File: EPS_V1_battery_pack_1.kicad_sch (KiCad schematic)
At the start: 16 parts, among them U1 MP2672AGD-0000-Z

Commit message: Minor fixes
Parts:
- R_MID: value 10k -> 0
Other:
- note added: "can't find value of R_MID on datasheet anywhere so I put 0 for now"
- note removed: "can't find value of R_MID on datasheet anywhere so I guessed 10k?"
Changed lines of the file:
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@@
 		)
 	)
-	(text "can't find value of R_MID on datasheet anywhere so I guessed 10k?"
+	(text "can't find value of R_MID on datasheet anywhere so I put 0 for now"
 		(exclude_from_sim no)
 		(at 156.21 134.366 0)
@@
 			)
 		)
-		(property "Value" "10k"
+		(property "Value" "0"
 			(at 122.682 86.36 0)
 			(effects

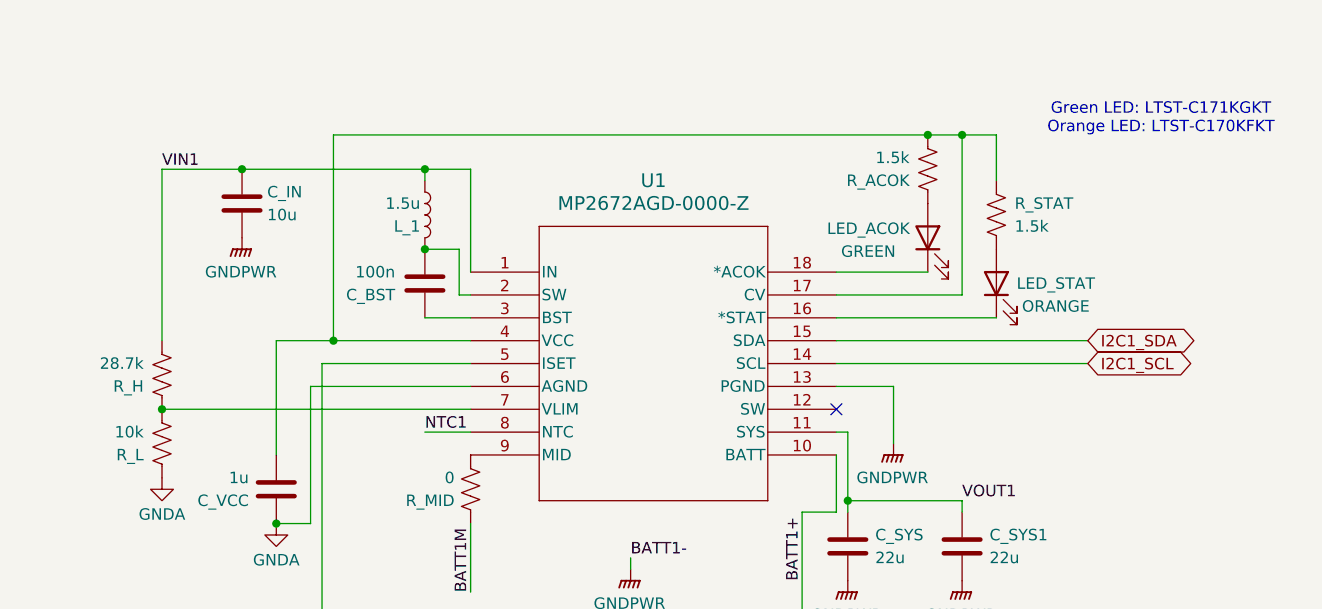
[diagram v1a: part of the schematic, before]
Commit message: Add solar to charger buck-boost converter, make charger standalone instead of host control
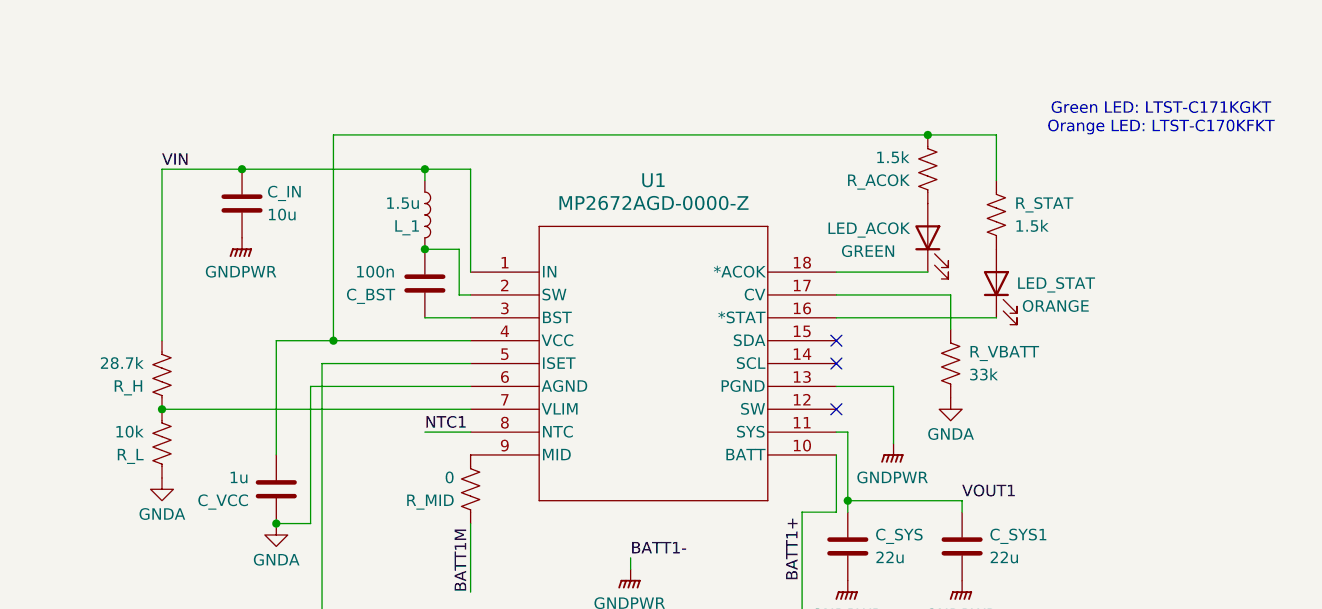
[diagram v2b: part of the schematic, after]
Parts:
- added R_VBATT: 33k, symbol Device:R_US
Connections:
- net GNDA: now also R_VBATT.2
- net at C_VCC.2, R_ACOK.2, R_STAT.1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: no longer U1.17 (CV)
- net I2C1_SCL: no longer names the net of U1.14 (SCL)
- net I2C1_SDA: no longer names the net of U1.15 (SDA)
- net VIN1 renamed VIN
- new net: R_VBATT.1, U1.17 (CV)
- no-connect marks 1 -> 3
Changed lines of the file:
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@@
-	)
-	(junction
-		(at 179.07 48.26)
-		(diameter 0)
-		(color 0 0 0 0)
 	)
 	(junction
@@
 		(at 165.1 78.74)
 	)
+	(no_connect
+		(at 165.1 73.66)
+	)
+	(no_connect
+		(at 165.1 71.12)
+	)
 	(wire
 		(pts
@@
 	(wire
 		(pts
-			(xy 182.88 48.26) (xy 179.07 48.26)
+			(xy 175.26 48.26) (xy 182.88 48.26)
 		)
 		(stroke
@@
 	(wire
 		(pts
+			(xy 177.8 66.04) (xy 177.8 69.85)
+		)
+		(stroke
+			(width 0)
+			(type default)
+		)
+	)
+	(wire
+		(pts
 			(xy 166.37 88.9) (xy 166.37 90.17)
 		)
@@
 	(wire
 		(pts
-			(xy 165.1 73.66) (xy 193.04 73.66)
-		)
-		(stroke
-			(width 0)
-			(type default)
-		)
-	)
-	(wire
-		(pts
 			(xy 109.22 71.12) (xy 124.46 71.12)
 		)
@@
 	(wire
 		(pts
-			(xy 179.07 48.26) (xy 175.26 48.26)
-		)
-		(stroke
-			(width 0)
-			(type default)
-		)
-	)
-	(wire
-		(pts
-			(xy 165.1 66.04) (xy 179.07 66.04)
-		)
-		(stroke
-			(width 0)
-			(type default)
-		)
-	)
-	(wire
-		(pts
 			(xy 165.1 68.58) (xy 182.88 68.58)
 		)
@@
 	(wire
 		(pts
-			(xy 179.07 66.04) (xy 179.07 48.26)
-		)
-		(stroke
-			(width 0)
-			(type default)
-		)
-	)
-	(wire
-		(pts
 			(xy 90.17 78.74) (xy 124.46 78.74)
 		)
@@
 	(wire
 		(pts
-			(xy 165.1 71.12) (xy 193.04 71.12)
-		)
-		(stroke
-			(width 0)
-			(type default)
-		)
-	)
-	(wire
-		(pts
 			(xy 166.37 81.28) (xy 166.37 88.9)
 		)
@@
 	(wire
 		(pts
+			(xy 165.1 66.04) (xy 177.8 66.04)
+		)
+		(stroke
+			(width 0)
+			(type default)
+		)
+	)
+	(wire
+		(pts
 			(xy 90.17 52.07) (xy 99.06 52.07)
 		)
@@
 		)
 	)
-	(label "VIN1"
+	(label "VIN"
 		(at 90.17 52.07 0)
 		(effects
@@
 			)
 			(justify left bottom)
-		)
-	)
-	(global_label "I2C1_SCL"
-		(shape bidirectional)
-		(at 193.04 73.66 0)
-		(fields_autoplaced yes)
-		(effects
-			(font
-				(size 1.27 1.27)
-			)
-			(justify left)
-		)
-		(property "Intersheetrefs" "${INTERSHEET_REFS}"
-			(at 205.9055 73.66 0)
-			(effects
-				(font
-					(size 1.27 1.27)
-				)
-				(justify left)
-				(hide yes)
-			)
-		)
-	)
-	(global_label "I2C1_SDA"
-		(shape bidirectional)
-		(at 193.04 71.12 0)
-		(fields_autoplaced yes)
-		(effects
-			(font
-				(size 1.27 1.27)
-			)
-			(justify left)
-		)
-		(property "Intersheetrefs" "${INTERSHEET_REFS}"
-			(at 205.966 71.12 0)
-			(effects
-				(font
-					(size 1.27 1.27)
-				)
-				(justify left)
-				(hide yes)
-			)
 		)
 	)
@@
 				(path "/85157432-5d03-48fa-ab40-27ed3d133f47/d6a7ca1d-fe68-467f-8233-74a5cf811189"
 					(reference "L_1")
+					(unit 1)
+				)
+			)
+		)
+	)
+	(symbol
+		(lib_id "Device:R_US")
+		(at 177.8 73.66 0)
+		(unit 1)
+		(exclude_from_sim no)
+		(in_bom yes)
+		(on_board yes)
+		(dnp no)
+		(property "Reference" "R_VBATT"
+			(at 179.832 72.39 0)
+			(effects
+				(font
+					(size 1.27 1.27)
+				)
+				(justify left)
+			)
+		)
+		(property "Value" "33k"
+			(at 179.832 74.93 0)
+			(effects
+				(font
+					(size 1.27 1.27)
+				)
+				(justify left)
+			)
+		)
+		(property "Footprint" ""
+			(at 178.816 73.914 90)
+			(effects
+				(font
+					(size 1.27 1.27)
+				)
+				(hide yes)
+			)
+		)
+		(property "Datasheet" "~"
+			(at 177.8 73.66 0)
+			(effects
+				(font
+					(size 1.27 1.27)
+				)
+				(hide yes)
+			)
+		)
+		(property "Description" "Resistor, US symbol"
+			(at 177.8 73.66 0)
+			(effects
+				(font
+					(size 1.27 1.27)
+				)
+				(hide yes)
+			)
+		)
+		(pin "2"
+		)
+		(pin "1"
+		)
+		(instances
+			(project "EPS_V1"
+				(path "/85157432-5d03-48fa-ab40-27ed3d133f47/d6a7ca1d-fe68-467f-8233-74a5cf811189"
+					(reference "R_VBATT")
 					(unit 1)
 				)
@@
 					(unit 1)
 				)
+			)
+		)
+	)
+	(symbol
+		(lib_id "power:GNDA")
+		(at 177.8 77.47 0)
+		(unit 1)
+		(exclude_from_sim no)
+		(in_bom yes)
+		(on_board yes)
+		(dnp no)
+		(property "Reference" "#PWR031"
+			(at 177.8 83.82 0)
+			(effects
+				(font
+					(size 1.27 1.27)
+				)
+				(hide yes)
+			)
+		)
+		(property "Value" "GNDA"
+			(at 177.8 81.534 0)
+			(effects
+				(font
+					(size 1.27 1.27)
+				)
+			)
+		)
+		(property "Footprint" ""
+			(at 177.8 77.47 0)
+			(effects
+				(font
+					(size 1.27 1.27)
+				)
+				(hide yes)
+			)
+		)
+		(property "Datasheet" ""
+			(at 177.8 77.47 0)
+			(effects
+				(font
+					(size 1.27 1.27)
+				)
+				(hide yes)
+			)
+		)
+		(property "Description" "Power symbol creates a global label with name \"GNDA\" , analog ground"
+			(at 177.8 77.47 0)
+			(effects
+				(font
+					(size 1.27 1.27)
+				)
+				(hide yes)
+			)
+		)
+		(pin "1"
+		)
+		(instances
+			(project "EPS_V1"
+				(path "/85157432-5d03-48fa-ab40-27ed3d133f47/d6a7ca1d-fe68-467f-8233-74a5cf811189"
+					(reference "#PWR031")
+					(unit 1)
+				)

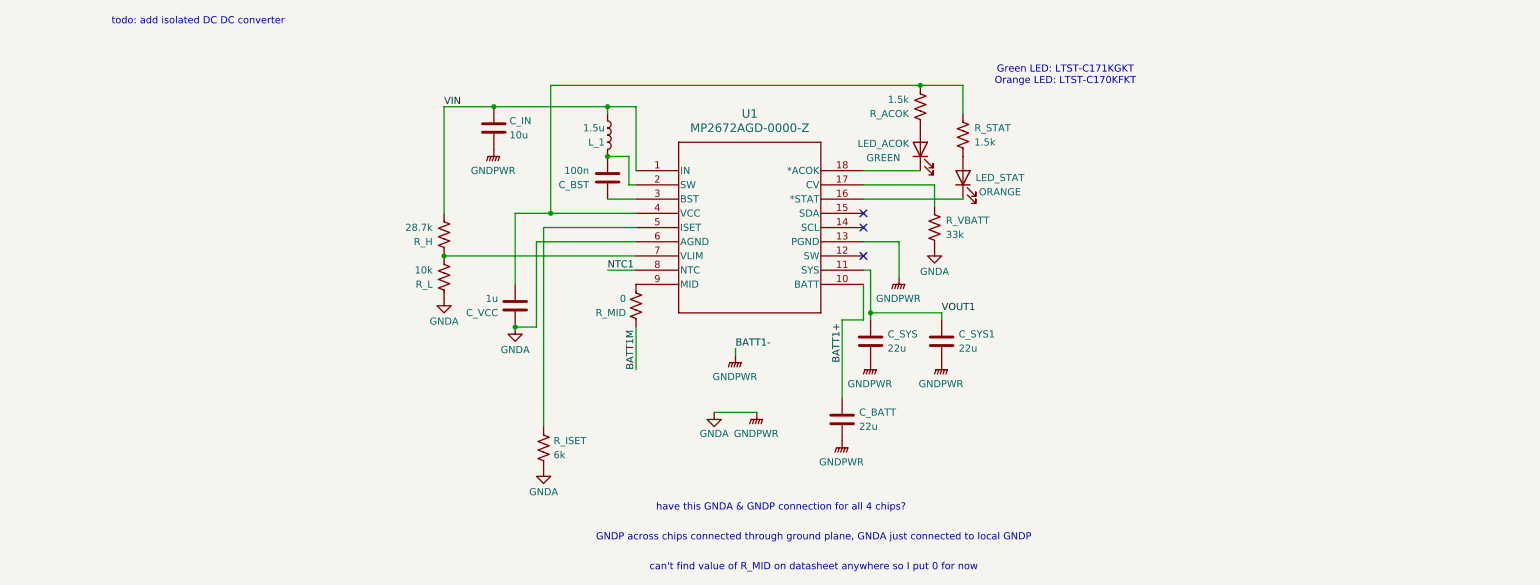
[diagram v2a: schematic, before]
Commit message: Add fuel gauge, fix voltage labels
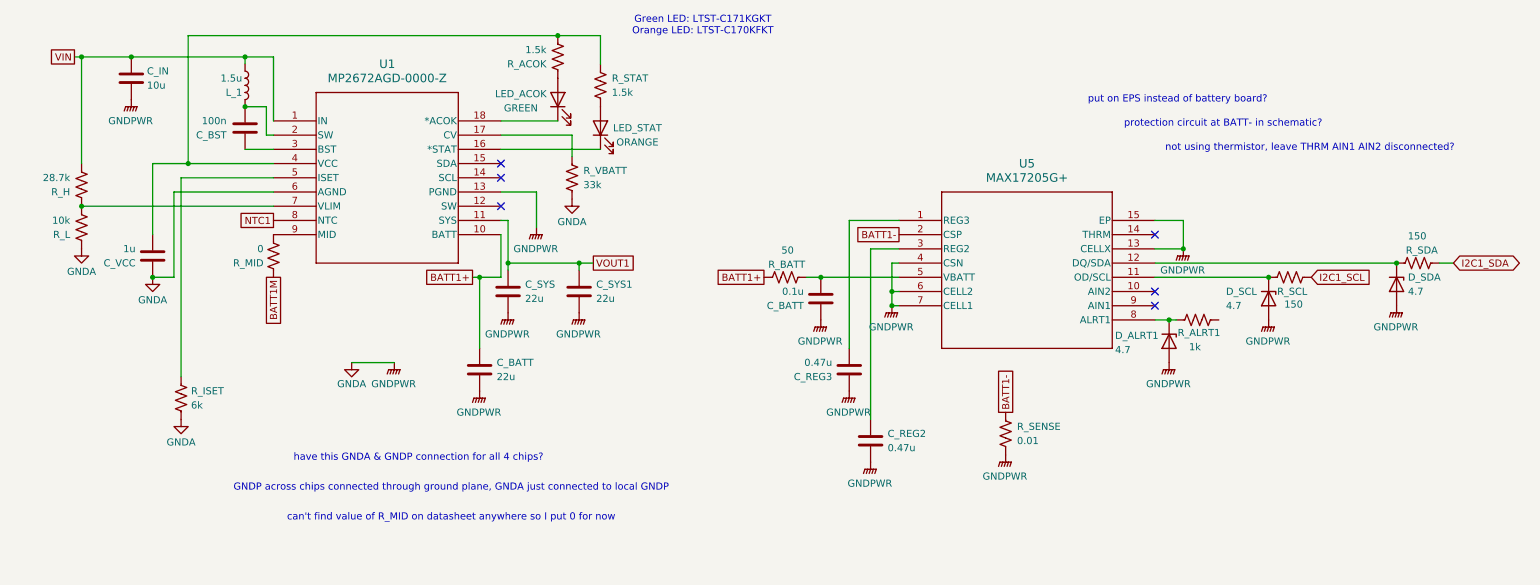
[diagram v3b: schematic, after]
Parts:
- added C_BATT: 0.1u, symbol Device:C
- added C_REG2, C_REG3: 0.47u, symbol Device:C
- added D_ALRT1, D_SCL, D_SDA: 4.7, symbol Device:D_Zener
- added R_ALRT1: 1k, symbol Device:R_US
- added R_BATT: 50, symbol Device:R_US
- added R_SCL, R_SDA: 150, symbol Device:R_US
- added R_SENSE: 0.01, symbol Device:R_US
- added U5: MAX17205G+, MAX17205G:21-0137_T1433&plus_2C_MXM, symbol MAX17205G:MAX17205G+
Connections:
- net BATT1+: now also R_BATT.1
- net GNDA: now also C_BATT.1, C_REG2.2, C_REG3.1, D_ALRT1.2 (A), D_SCL.2 (A), D_SDA.2 (A), R_SENSE.2, U5.13 (CELLX), U5.15 (EP), U5.4 (CSN), U5.6 (CELL2), U5.7 (CELL1)
- new net: D_SDA.1 (K), R_SDA.1, U5.12 (DQ/SDA)
- new net: C_BATT.2, R_BATT.2, U5.5 (VBATT)
- new net: D_ALRT1.1 (K), R_ALRT1.1, U5.8 (ALRT1)
- new net: C_REG3.2, U5.1 (REG3)
- new net: D_SCL.1 (K), R_SCL.1, U5.11 (OD/SCL)
- new net: C_REG2.1, U5.3 (REG2)
- new net BATT1-: R_SENSE.1, U5.2 (CSP)
- new net I2C1_SCL: R_SCL.2
- new net I2C1_SDA: R_SDA.2
- no-connect marks 3 -> 6
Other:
- note added: "not using thermistor, leave THRM AIN1 AIN2 disconnected?"
- note added: "protection circuit at BATT- in schematic?"
- note added: "put on EPS instead of battery board?"
- note removed: "todo: add isolated DC DC converter"
- moved on the sheet: C_BATT, C_BST, C_IN, C_SYS, C_SYS1, C_VCC, LED_ACOK, LED_STAT, L_1, R_ACOK, R_H, R_ISET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
